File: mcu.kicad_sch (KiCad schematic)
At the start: 29 parts, among them J4 Conn_02x05_Odd_Even, U7 STM32F407VGTx, U8 STM809SWX6F, Y1 8MHz

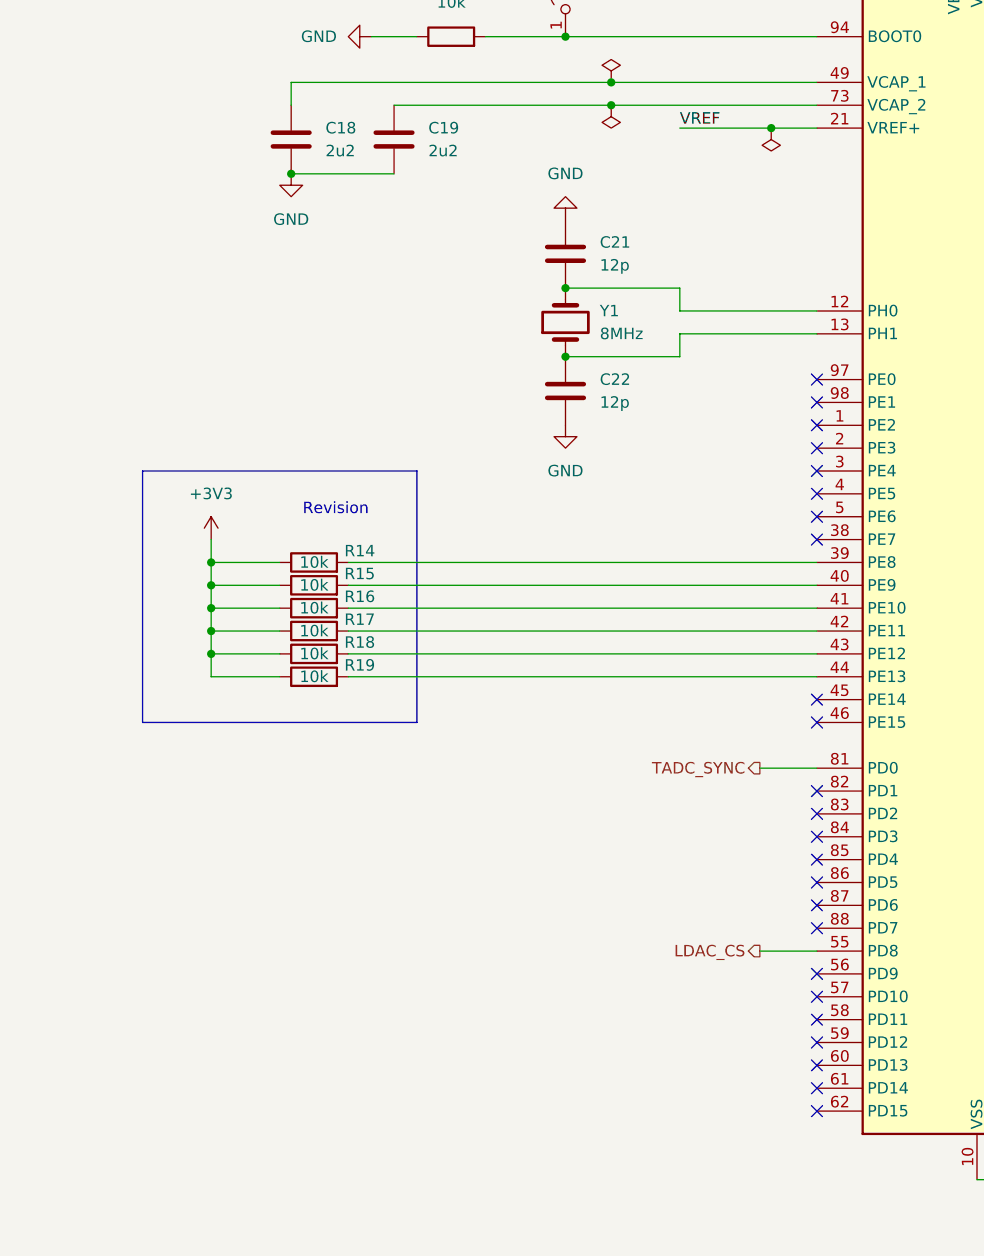
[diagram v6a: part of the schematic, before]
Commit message: add V01 production files, bug fixes
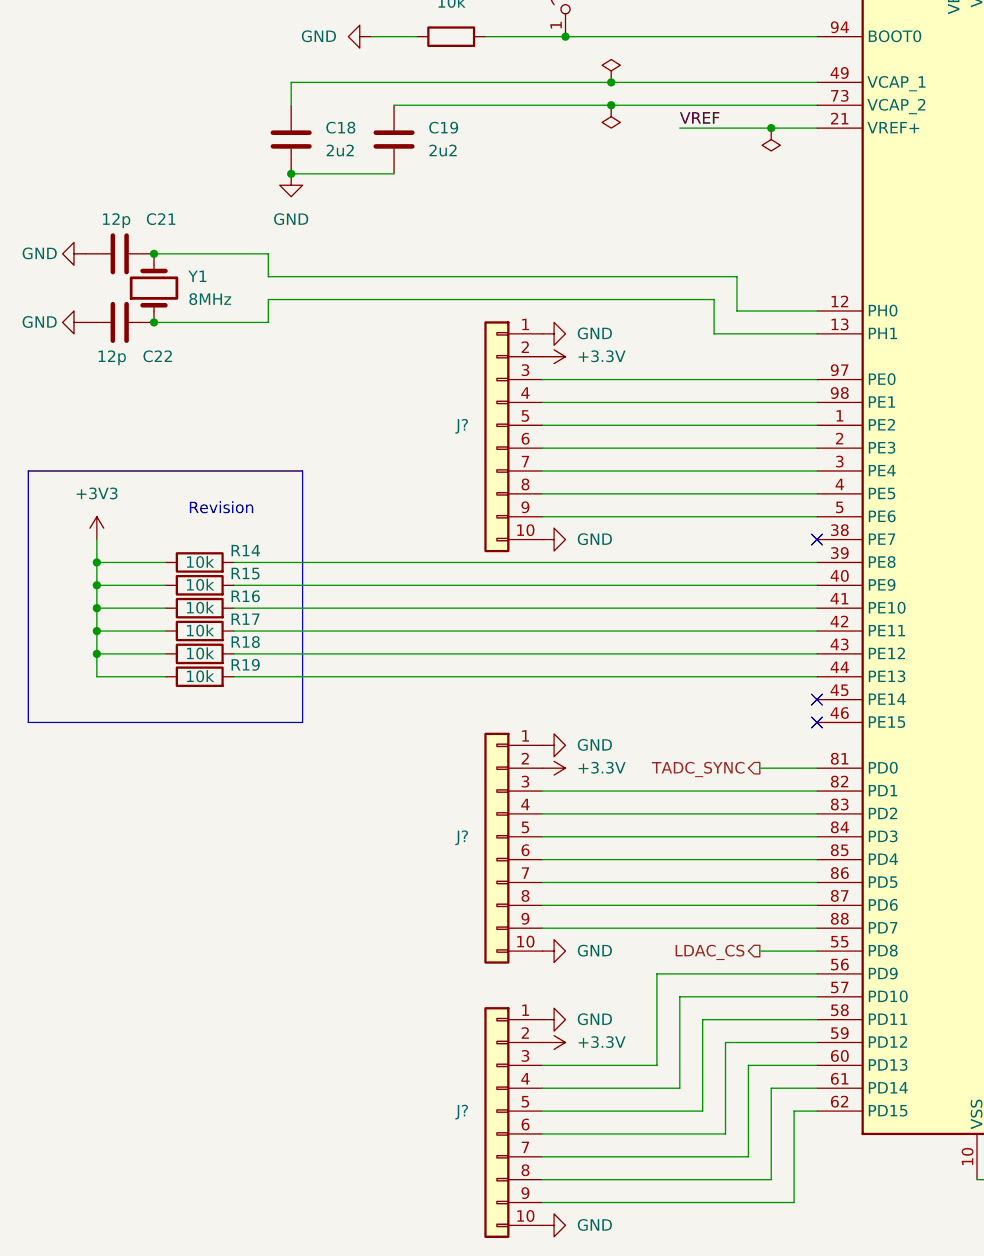
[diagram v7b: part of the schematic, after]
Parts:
- added J? (x3): Conn_01x10, symbol Connector_Generic:Conn_01x10
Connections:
- net +3V3: now also J?.2 (Pin_2), J?.2 (Pin_2), J?.2 (Pin_2)
- net GND: now also J?.1 (Pin_1), J?.1 (Pin_1), J?.1 (Pin_1), J?.10 (Pin_10), J?.10 (Pin_10), J?.10 (Pin_10)
- net at U7.1 (PE2): now also J?.5 (Pin_5)
- net at U7.2 (PE3): now also J?.6 (Pin_6)
- net at U7.3 (PE4): now also J?.7 (Pin_7)
- net at U7.4 (PE5): now also J?.8 (Pin_8)
- net at U7.5 (PE6): now also J?.9 (Pin_9)
- net at U7.56 (PD9): now also J?.3 (Pin_3)
- net at U7.57 (PD10): now also J?.4 (Pin_4)
- net at U7.58 (PD11): now also J?.5 (Pin_5)
- net at U7.59 (PD12): now also J?.6 (Pin_6)
- net at U7.60 (PD13): now also J?.7 (Pin_7)
- net at U7.61 (PD14): now also J?.8 (Pin_8)
- net at U7.62 (PD15): now also J?.9 (Pin_9)
- net at U7.82 (PD1): now also J?.3 (Pin_3)
- net at U7.83 (PD2): now also J?.4 (Pin_4)
- net at U7.84 (PD3): now also J?.5 (Pin_5)
- net at U7.85 (PD4): now also J?.6 (Pin_6)
- net at U7.86 (PD5): now also J?.7 (Pin_7)
- net at U7.87 (PD6): now also J?.8 (Pin_8)
- net at U7.88 (PD7): now also J?.9 (Pin_9)
- net at U7.97 (PE0): now also J?.3 (Pin_3)
- net at U7.98 (PE1): now also J?.4 (Pin_4)
- no-connect marks 40 -> 19
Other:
- moved on the sheet: C21, C22, R14, R15, R16, R17, R18, R19, Y1

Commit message: v 0.2 schematics
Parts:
- removed J? (x3): Conn_01x10, symbol Connector_Generic:Conn_01x10
- added J? (x2): Conn_01x10, symbol Connector_Generic:Conn_01x10
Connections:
- net +3V3: now also J?.2 (Pin_2)
- net GND: now also J?.1 (Pin_1), J?.10 (Pin_10)
- net LD_EN: now reaches U7.56 (PD9)
- net at U7.57 (PD10): now also J?.1 (Pin_1)
- net at U7.58 (PD11): now also J?.2 (Pin_2)
- net at U7.59 (PD12): now also J?.3 (Pin_3)
- net at U7.60 (PD13): now also J?.4 (Pin_4)
- net at U7.61 (PD14): now also J?.5 (Pin_5)
- net at U7.62 (PD15): now also J?.6 (Pin_6)
- net at U7.63 (PC6): now also J?.7 (Pin_7)
- net at U7.64 (PC7): now also J?.8 (Pin_8)
- net at U7.65 (PC8): now also J?.9 (Pin_9)
- net at U7.66 (PC9): now also J?.10 (Pin_10)
- net at U7.82 (PD1): now also J?.3 (Pin_3)
- net at U7.83 (PD2): now also J?.4 (Pin_4)
- net at U7.84 (PD3): now also J?.5 (Pin_5)
- net at U7.85 (PD4): now also J?.6 (Pin_6)
- net at U7.86 (PD5): now also J?.7 (Pin_7)
- net at U7.87 (PD6): now also J?.8 (Pin_8)
- net at U7.88 (PD7): now also J?.9 (Pin_9)
- no-connect marks 19 -> 22
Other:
- moved on the sheet: C21, C22, R14, R15, R16, R17, R18, R19, Y1
